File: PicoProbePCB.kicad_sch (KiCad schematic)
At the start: 3 parts, among them J1 Conn_01x03_Socket, U1 RaspberryPi_Pico_SecondaryPins, U2 RaspberryPi_Pico

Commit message: add optional smt power led on top layer
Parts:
- added D1: LED, LED_SMD:LED_0603_1608Metric_Pad1.05x0.95mm_HandSolder, symbol Device:LED
- added R1: R, LED_SMD:LED_0603_1608Metric_Pad1.05x0.95mm_HandSolder, symbol Device:R
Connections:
- net GND: now also D1.1 (K)
- net VCC: now also R1.1
- new net: D1.2 (A), R1.2
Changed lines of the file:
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@@
+    )
+  )
+  (symbol (lib_id "Device:LED") (at 80.01 39.37 90) (unit 1)
+    (in_bom yes) (on_board yes) (dnp no) (fields_autoplaced)
+    (property "Reference" "D1" (at 82.931 39.7454 90)
+      (effects (font (size 1.27 1.27)) (justify right))
+    )
+    (property "Value" "LED" (at 82.931 42.1696 90)
+      (effects (font (size 1.27 1.27)) (justify right))
+    )
+    (property "Footprint" "LED_SMD:LED_0603_1608Metric_Pad1.05x0.95mm_HandSolder" (at 80.01 39.37 0)
+      (effects (font (size 1.27 1.27)) hide)
+    )
+    (property "Datasheet" "~" (at 80.01 39.37 0)
+      (effects (font (size 1.27 1.27)) hide)
+    )
+    (pin "1")
+    (pin "2")
+    (instances
+      (project "PicoProbePCB"
+        (path "/d65d41a8-1250-4204-950e-de0b29d996bc"
+          (reference "D1") (unit 1)
+        )
+      )
+    )
+  )
+  (symbol (lib_id "power:VCC") (at 80.01 27.94 0) (unit 1)
+    (in_bom yes) (on_board yes) (dnp no) (fields_autoplaced)
+    (property "Reference" "#PWR06" (at 80.01 31.75 0)
+      (effects (font (size 1.27 1.27)) hide)
+    )
+    (property "Value" "VCC" (at 80.01 23.8069 0)
+      (effects (font (size 1.27 1.27)))
+    )
+    (property "Footprint" "" (at 80.01 27.94 0)
+      (effects (font (size 1.27 1.27)) hide)
+    )
+    (property "Datasheet" "" (at 80.01 27.94 0)
+      (effects (font (size 1.27 1.27)) hide)
+    )
+    (pin "1")
+    (instances
+      (project "PicoProbePCB"
+        (path "/d65d41a8-1250-4204-950e-de0b29d996bc"
+          (reference "#PWR06") (unit 1)
+        )
+      )
     )
   )
@@
         )
       )
+    )
+  )
+  (symbol (lib_id "power:GND") (at 80.01 43.18 0) (unit 1)
+    (in_bom yes) (on_board yes) (dnp no) (fields_autoplaced)
+    (property "Reference" "#PWR07" (at 80.01 49.53 0)
+      (effects (font (size 1.27 1.27)) hide)
+    )
+    (property "Value" "GND" (at 80.01 47.3131 0)
+      (effects (font (size 1.27 1.27)))
+    )
+    (property "Footprint" "" (at 80.01 43.18 0)
+      (effects (font (size 1.27 1.27)) hide)
+    )
+    (property "Datasheet" "" (at 80.01 43.18 0)
+      (effects (font (size 1.27 1.27)) hide)
+    )
+    (pin "1")
+    (instances
+      (project "PicoProbePCB"
+        (path "/d65d41a8-1250-4204-950e-de0b29d996bc"
+          (reference "#PWR07") (unit 1)
+        )
+      )
+    )
+  )
+  (symbol (lib_id "Device:R") (at 80.01 31.75 0) (unit 1)
+    (in_bom yes) (on_board yes) (dnp no) (fields_autoplaced)
+    (property "Reference" "R1" (at 81.788 30.5379 0)
+      (effects (font (size 1.27 1.27)) (justify left))
+    )
+    (property "Value" "R" (at 81.788 32.9621 0)
+      (effects (font (size 1.27 1.27)) (justify left))
+    )
+    (property "Footprint" "LED_SMD:LED_0603_1608Metric_Pad1.05x0.95mm_HandSolder" (at 78.232 31.75 90)
+      (effects (font (size 1.27 1.27)) hide)
+    )
+    (property "Datasheet" "~" (at 80.01 31.75 0)
+      (effects (font (size 1.27 1.27)) hide)
+    )
+    (pin "2")
+    (pin "1")
+    (instances
+      (project "PicoProbePCB"
+        (path "/d65d41a8-1250-4204-950e-de0b29d996bc"
+          (reference "R1") (unit 1)
+        )
+      )

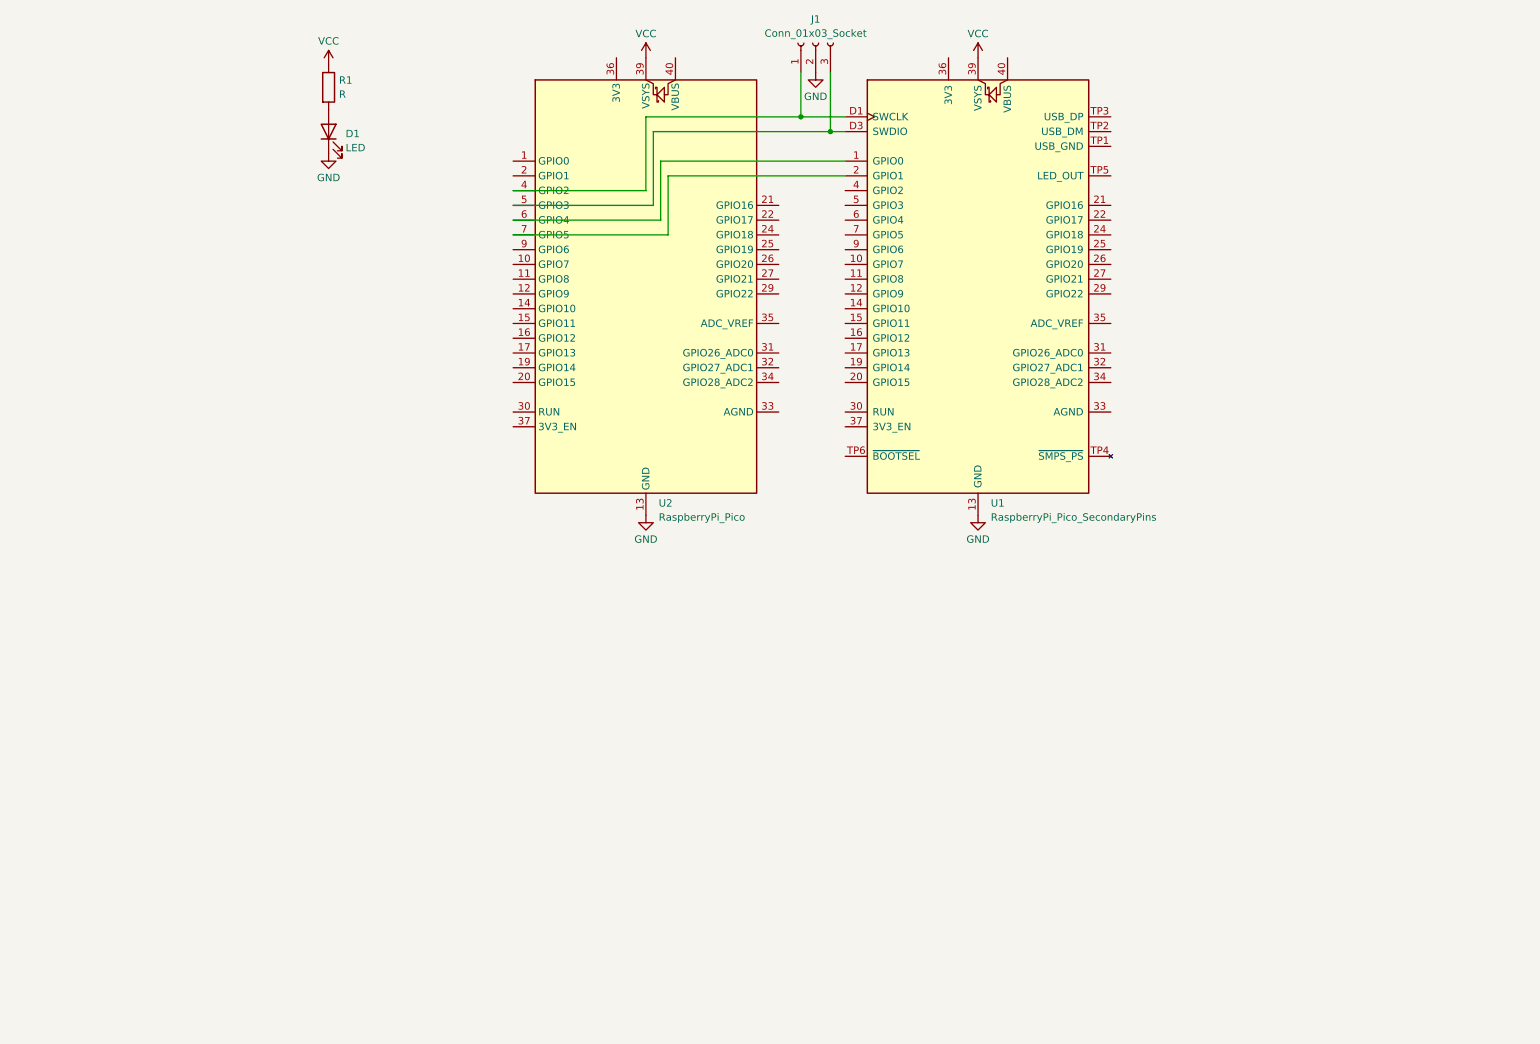
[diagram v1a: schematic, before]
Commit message: update to kicad 8.0 and add top-layer (optional) power rail breakout
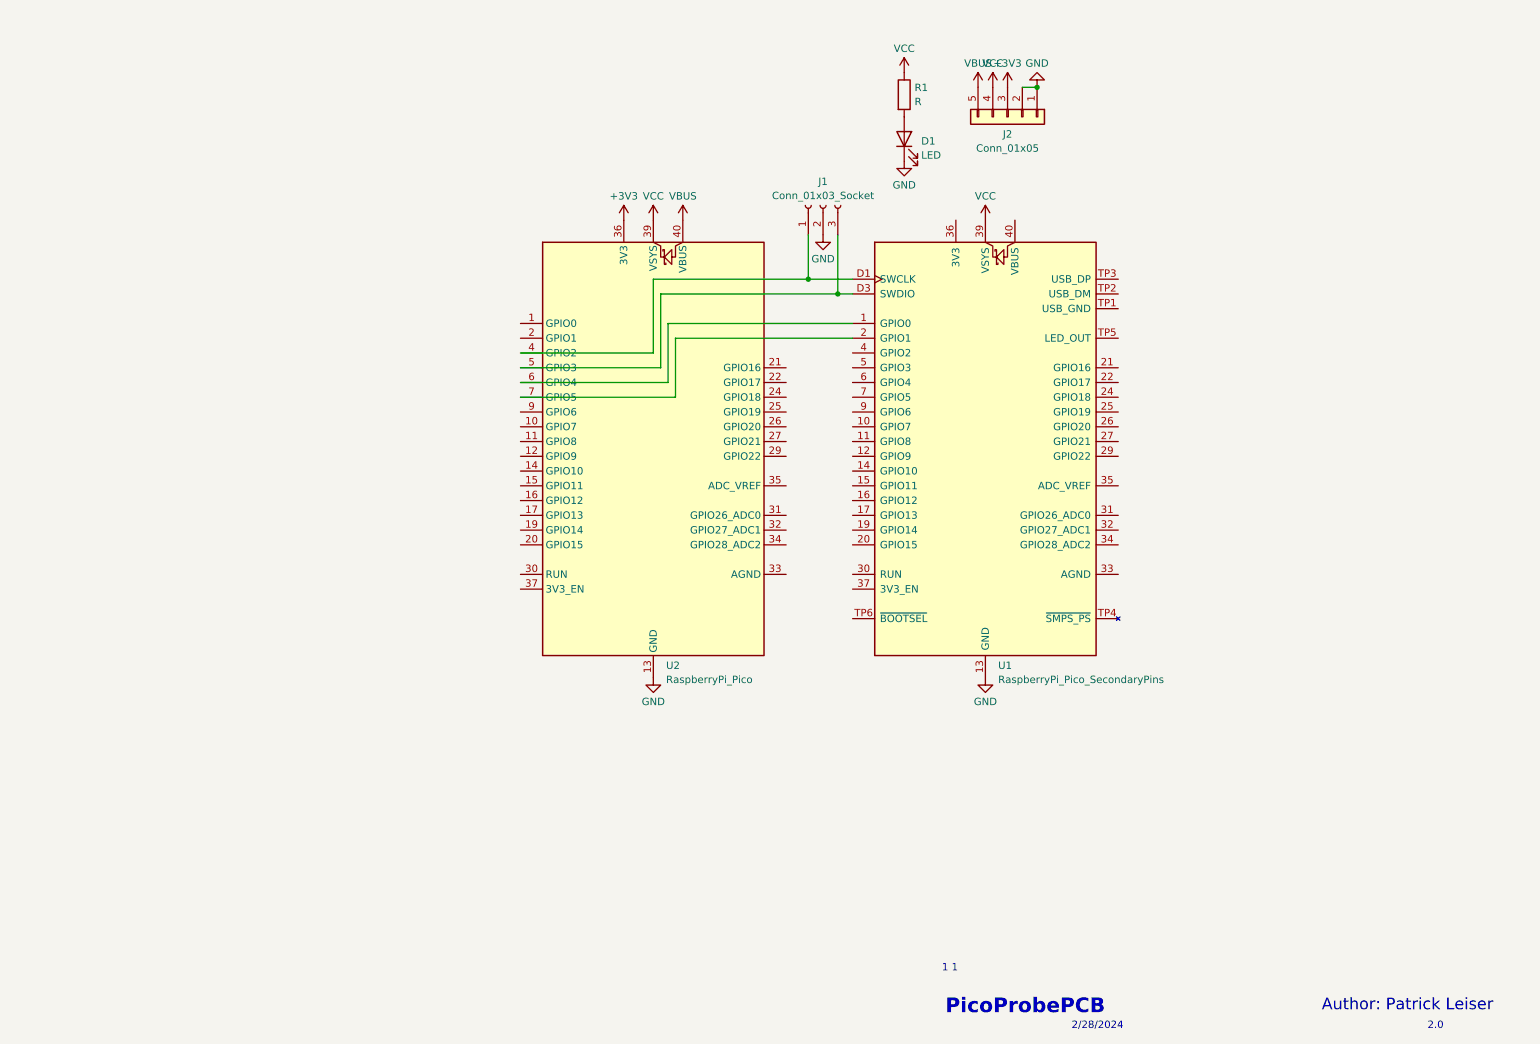
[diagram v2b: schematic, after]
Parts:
- added J2: Conn_01x05, Connector_PinHeader_2.54mm:PinHeader_1x05_P2.54mm_Vertical_SMD_Pin1Left, symbol Connector_Generic:Conn_01x05
- U1, U2: footprint Module_RaspberryPi_Pico:RaspberryPi_Pico_Debug_PicoProbePinsOnlyLargePads -> RaspberryPi_Pico:RaspberryPi_Pico_Debug_PicoProbePinsOnlyLargePads
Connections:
- net GND: now also J2.1 (Pin_1), J2.2 (Pin_2)
- net VCC: now also J2.4 (Pin_4)
- net +3V3: now reaches U2.36 (3V3)
- net +3V3: now also J2.3 (Pin_3)
- net VBUS: now reaches U2.40 (VBUS)
- net VBUS: now also J2.5 (Pin_5)
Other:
- note added: "1 1"
- note added: "2.0"
- note added: "2/28/2024"
- note added: "Author: Patrick Leiser"
- note added: "PicoProbePCB"
- moved on the sheet: D1, J1, R1, U1, U2

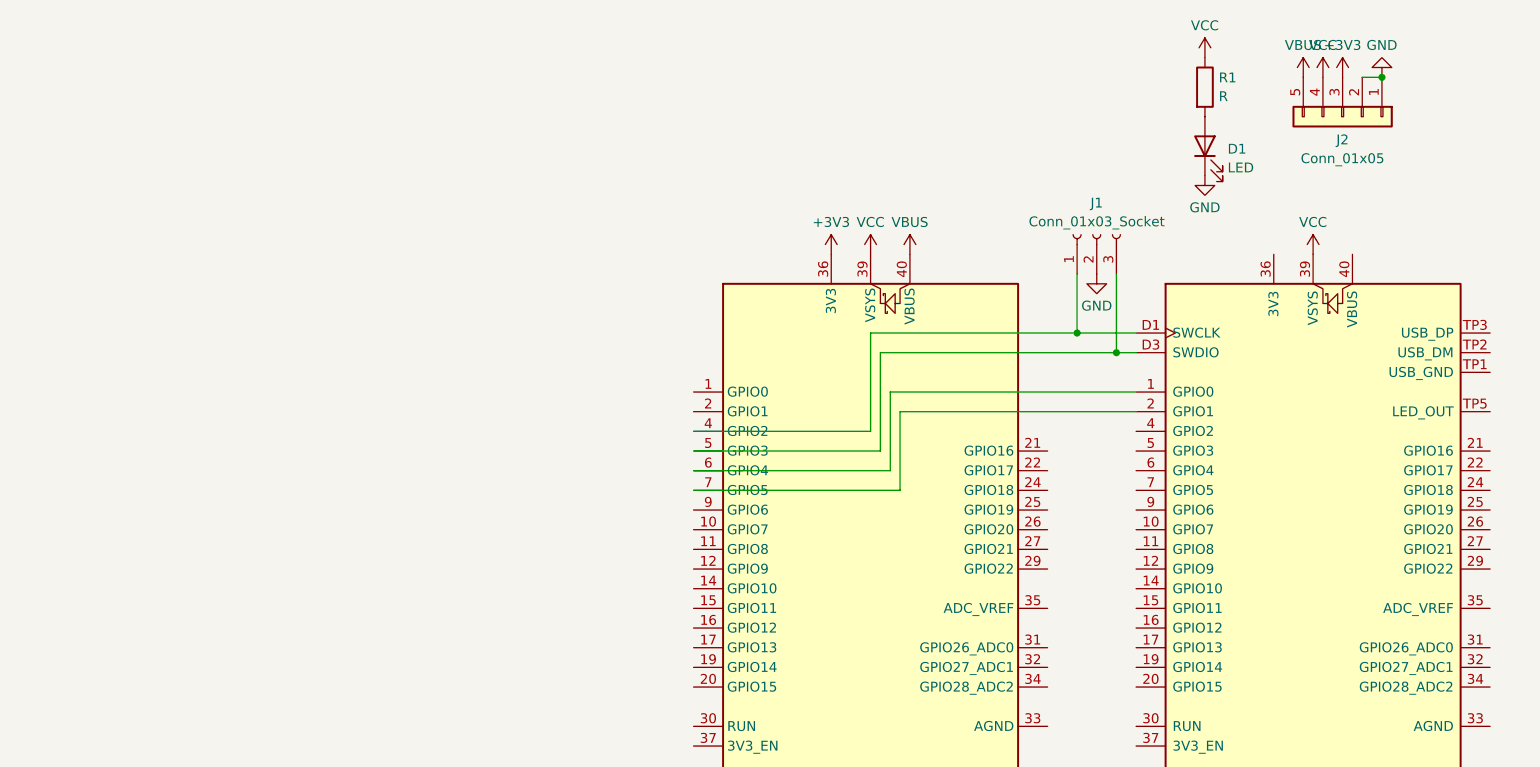
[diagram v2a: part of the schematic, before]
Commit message: add readme and images
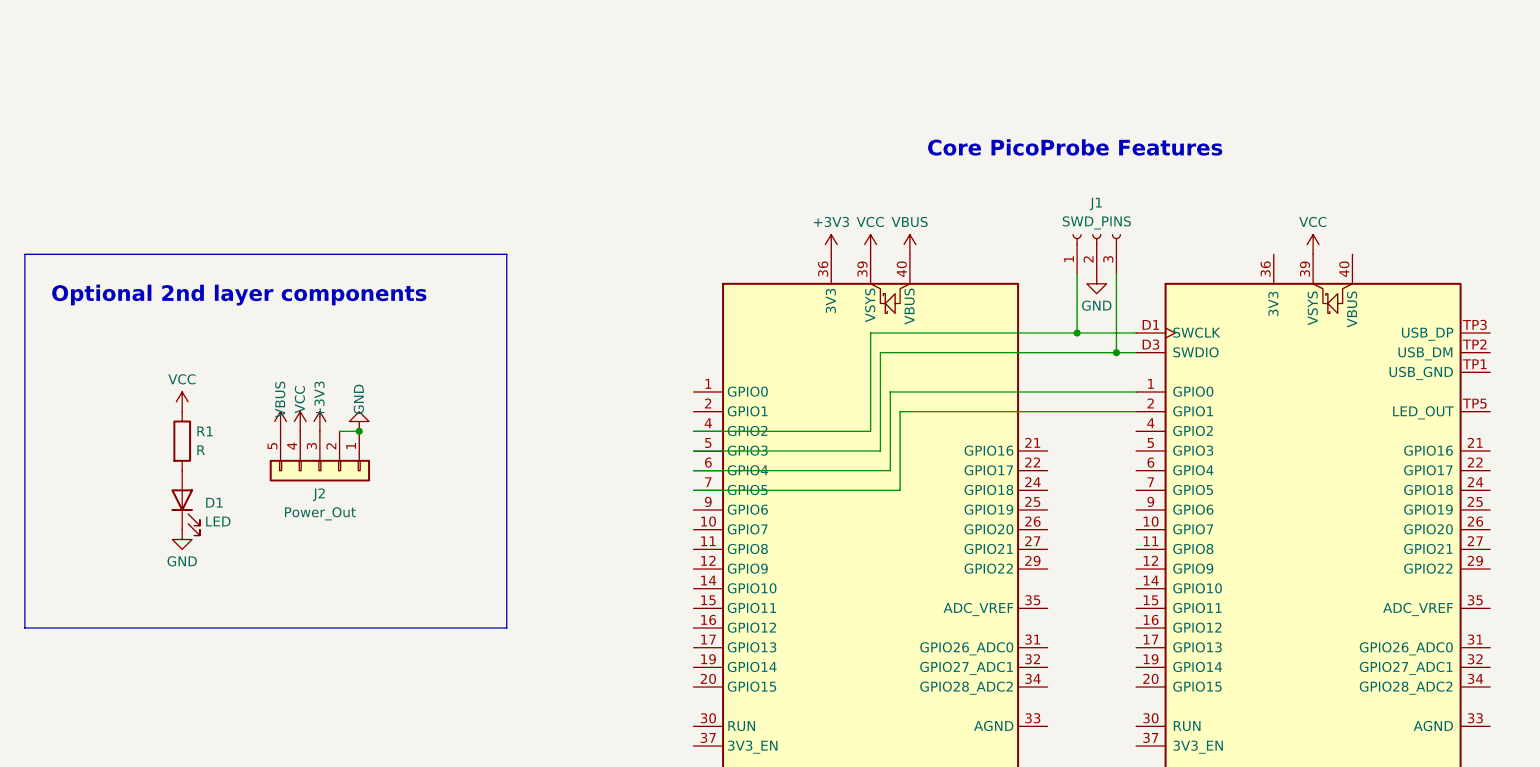
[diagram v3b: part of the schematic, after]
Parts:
- J1: value Conn_01x03_Socket -> SWD_PINS
- J2: value Conn_01x05 -> Power_Out
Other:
- note added: "Core PicoProbe Features"
- note added: "Optional 2nd layer components"
- moved on the sheet: D1, J2, R1
